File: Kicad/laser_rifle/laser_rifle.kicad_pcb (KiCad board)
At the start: 2 copper layers, 56 x 15 mm, 27 parts, among them J1 Screw_Terminal_01x02, J3 USB_C_Receptacle_PowerOnly_6P, Q1 MMBT3904, SW1 SW_DIP_x01, SW2 SW_DIP_x01, SW3 SW_DIP_x01, U1 MCP1700x-300xxTT, U2 ATtiny85V-10P, U3 BQ21040

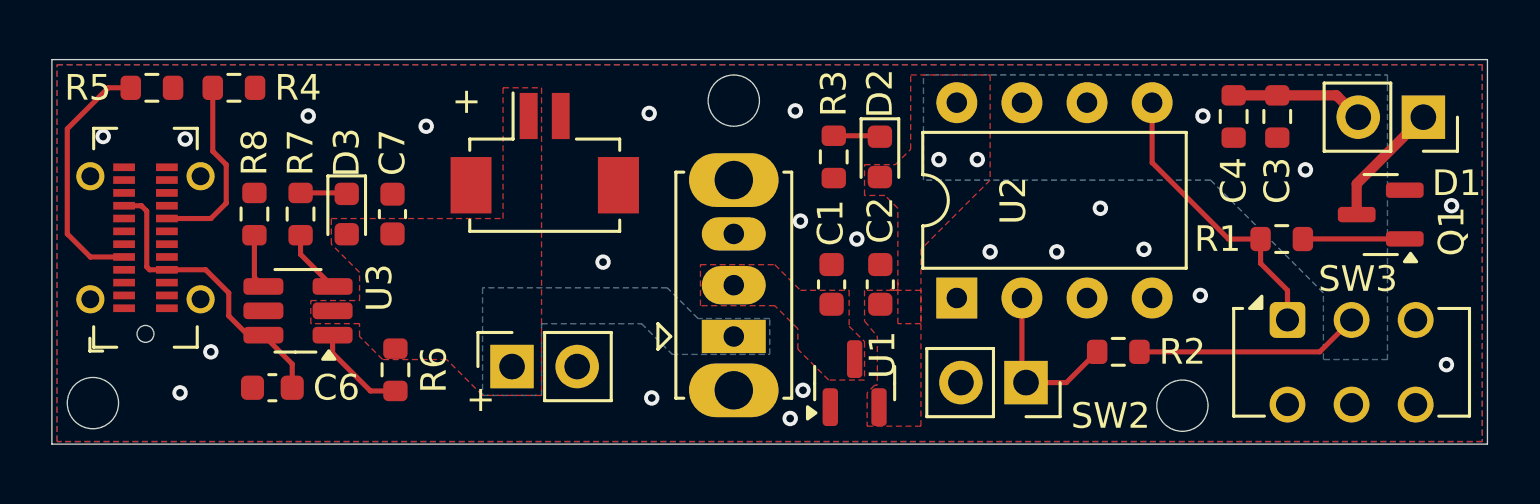
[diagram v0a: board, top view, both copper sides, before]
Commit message: Aggiornata pcb e creata pcb 48mm
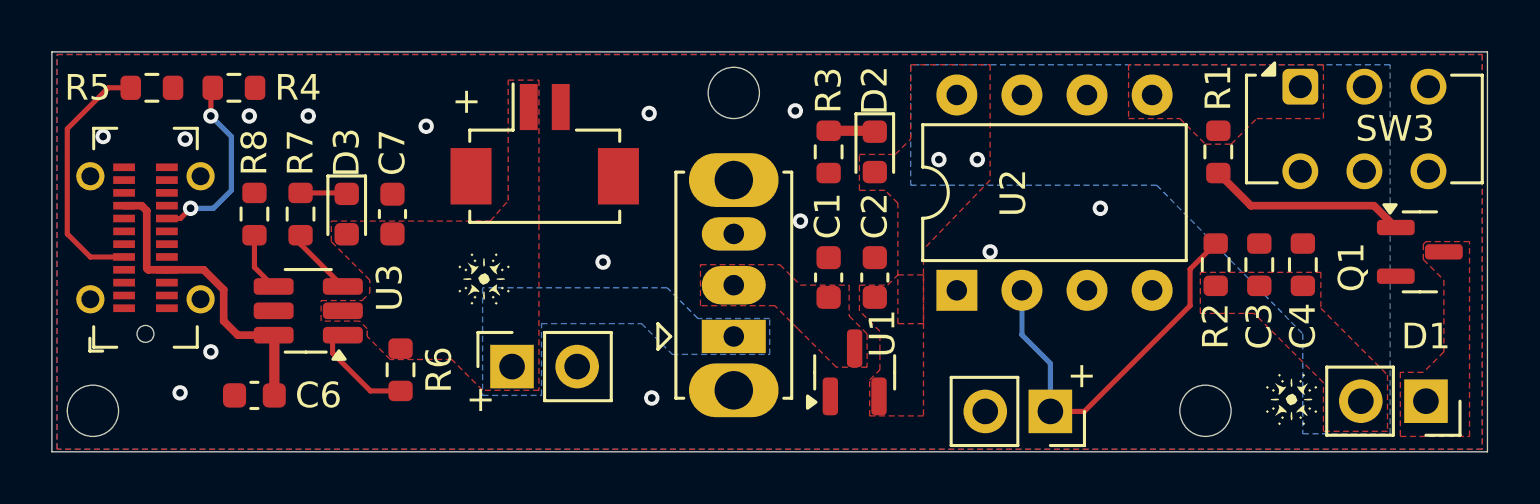
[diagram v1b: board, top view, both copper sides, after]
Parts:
- added G***: LOGO, laser_rifle:laser, F.Cu at (86.8, 103.5)
- added G***: LOGO, laser_rifle:laser, F.Cu at (118.3, 108.2)
- moved D1 11.1 mm to (123.6, 108.3)
- moved SW3 9.11 mm to (118.7, 96.1)
- moved C4 6.38 mm to (118.8, 103.0), turned to 90 degrees
- moved C3 5.82 mm to (117.1, 103.0), turned to 90 degrees
- moved R2 5.10 mm to (115.4, 103.0), turned to 90 degrees
- moved R1 4.21 mm to (115.5, 98.6), turned to -90 degrees
- moved Q1 2.11 mm to (123.4, 102.5), turned to 0 degrees
- moved SW2 1.47 mm to (109.0, 108.7)
- moved C6 0.76 mm to (77.9, 108.1)
- moved U1 0.42 mm to (101.3, 107.2)
- moved U3 0.40 mm to (80.0, 104.8)
- moved BT2 0.35 mm to (89.2, 98.3)
- moved C2 0.35 mm to (102.1, 103.5)
- moved U2 0.30 mm to (105.3, 104.0)
- moved C1 0.29 mm to (100.3, 103.5)
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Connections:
- SW1 pad : (no net) -> GND
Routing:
- net VCC: track 13.9 -> 0.00 mm
- net laser: track 11.3 -> 0.00 mm
- net trigger: track 6.52 -> 15.2 mm
- net Net-(D1-K): track 4.88 -> 0.00 mm
- net Net-(Q1-B): track 3.98 -> 7.81 mm
- net Net-(J3-CC2): track 7.28 -> 7.23 mm, vias 0 -> 2
- net GND: vias 23 -> 14
- added copper zone on F.Cu, net Net-(D1-K)
- added copper zone on F.Cu, net laser
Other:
- board size 56 x 15 mm -> 56 x 15.6 mm
- board text added: "Dade3e Laser_rifle"
